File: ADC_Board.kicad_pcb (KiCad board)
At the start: 4 copper layers, 100 x 100 mm, 226 parts, among them J10 Wire_Solder_2Pin, J11 Wire_Solder_2Pin, J12 Wire_Solder_2Pin, J3 Conn_01x04_Pin, J4 Conn_01x04_Pin, J5 Conn_01x04_Pin, J6 Conn_01x04_Pin, J7 Wire_Solder_2Pin, J8 Wire_Solder_2Pin, J9 Conn_01x07_Socket, Q10 NVMFS5C468NL-HXY, Q11 NVMFS5C468NL-HXY, Q12 NVMFS5C468NL-HXY, Q4 DOD40P03, Q5 NVMFS5C468NL-HXY, Q6 NVMFS5C468NL-HXY, Q7 NVMFS5C468NL-HXY, Q8 NVMFS5C468NL-HXY, Q9 NVMFS5C468NL-HXY, SW1 SW_Push, U1 TPS70933DBVR, U10 INA281A3, U11 INA281A3, U12 INA281A3, U2 STM32G030K6Tx, U3 LM5109BMA, U4 LM5109BMA, U5 LM5109BMA, U6 LM5109BMA, U7 INA281A3, U8 SN74HCS08PWR, U9 SN74HCS02PWR, Y1 HSO321S 16MHZ 3.3V

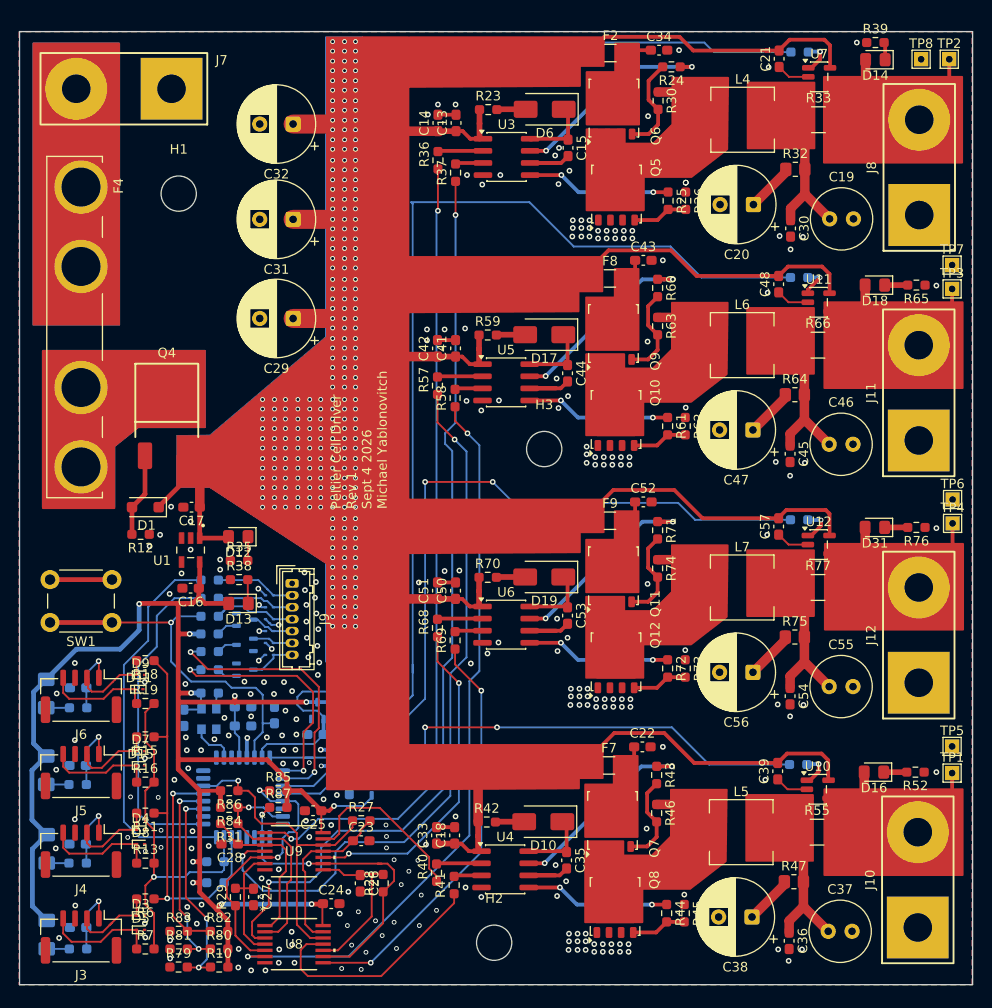
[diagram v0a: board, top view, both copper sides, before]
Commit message: changed I2C temp sensor to thermistor
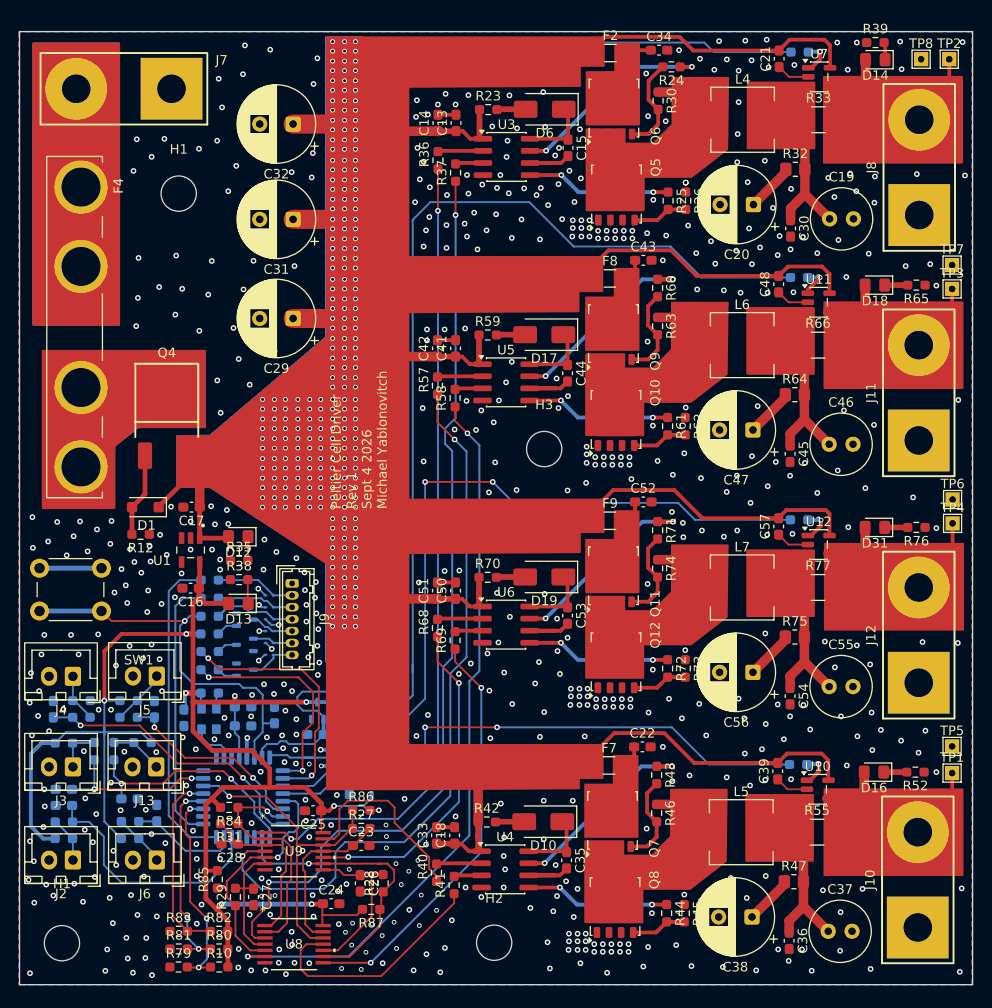
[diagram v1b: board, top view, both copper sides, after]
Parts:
- removed C11: 1u, Capacitor_SMD:C_0603_1608Metric_Pad1.08x0.95mm_HandSolder
- removed D11, D15, D3, D4, D5, D7, D8, D9: ESD9B3.3ST5G, Diode_SMD:D_SOD-923
- removed F1, F3, F5, F6: 25mA, Fuse:Fuse_1206_3216Metric_Pad1.42x1.75mm_HandSolder
- removed R16, R17, R18, R19, R20: 100r, Resistor_SMD:R_0603_1608Metric_Pad0.98x0.95mm_HandSolder
- removed R21, R22: 4.7k, Resistor_SMD:R_0603_1608Metric_Pad0.98x0.95mm_HandSolder
- added C1: 1u, Capacitor_SMD:C_0603_1608Metric_Pad1.08x0.95mm_HandSolder, B.Cu at (44.2, 152.7)
- added C2: 1u, Capacitor_SMD:C_0603_1608Metric_Pad1.08x0.95mm_HandSolder, B.Cu at (44.2, 151.0)
- added C3: 1u, Capacitor_SMD:C_0603_1608Metric_Pad1.08x0.95mm_HandSolder, B.Cu at (43.1, 142.6)
- added H1: MountingHole, MountingHole:MountingHole_3.7mm, F.Cu at (44.0, 167.2)
- added J13: Conn_01x02_Pin, Connector_JST:JST_XH_B2B-XH-A_1x02_P2.50mm_Vertical, F.Cu at (53.9, 148.7)
- added J2: Conn_01x02_Pin, Connector_JST:JST_XH_B2B-XH-A_1x02_P2.50mm_Vertical, F.Cu at (45.1, 158.4)
- added R1: 10k, Resistor_SMD:R_0603_1608Metric_Pad0.98x0.95mm_HandSolder, B.Cu at (44.2, 156.2)
- added R2: 1k, Resistor_SMD:R_0603_1608Metric_Pad0.98x0.95mm_HandSolder, B.Cu at (44.2, 154.4)
- added R3: 10k, Resistor_SMD:R_0603_1608Metric_Pad0.98x0.95mm_HandSolder, B.Cu at (44.2, 146.2)
- added R4: 1k, Resistor_SMD:R_0603_1608Metric_Pad0.98x0.95mm_HandSolder, B.Cu at (47.4, 147.0)
- added R5: 10k, Resistor_SMD:R_0603_1608Metric_Pad0.98x0.95mm_HandSolder, B.Cu at (46.0, 141.7)
- J3, J4, J5, J6: value Conn_01x04_Pin -> Conn_01x02_Pin; footprint Connector_JST:JST_GH_BM04B-GHS-TBT_1x04-1MP_P1.25mm_Vertical -> Connector_JST:JST_XH_B2B-XH-A_1x02_P2.50mm_Vertical
- R11, R7: value 100r -> 10k; moved to B.Cu
- R13, R15, R6: value 100r -> 1k; moved to B.Cu
- R14: value 100r -> 10k
- R8: value 100r -> 1k
- moved R7 26.1 mm to (51.0, 141.7), turned to 180 degrees
- moved R8 24.9 mm to (51.0, 143.4), turned to 0 degrees
- moved C5 24.3 mm to (53.7, 142.6), turned to 90 degrees
- moved R6 20.2 mm to (46.0, 143.4)
- moved J6 18.9 mm to (54.0, 158.4)
- moved J4 18.4 mm to (45.1, 139.2)
- moved J3 17.9 mm to (45.1, 148.7)
- moved R87 14.5 mm to (76.5, 163.6), turned to 180 degrees
- moved R14 14.4 mm to (52.5, 146.1), turned to 0 degrees
- moved R86 14.0 mm to (75.4, 153.2), turned to 0 degrees
- moved J5 12.9 mm to (54.0, 139.1)
- moved R85 11.3 mm to (60.3, 160.4), turned to 90 degrees
- moved C7 8.91 mm to (54.0, 153.5), turned to 90 degrees
- moved C10 6.48 mm to (51.1, 152.0), turned to 0 degrees
- moved R13 4.66 mm to (51.1, 154.4)
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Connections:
- net ADC_1 renamed ADC_MOTOR_CURRENT_1
- net ADC_2 renamed ADC_MOTOR_CURRENT_2
- net ADC_3 renamed ADC_MOTOR_CURRENT_3
- net ADC_4 renamed ADC_MOTOR_CURRENT_4
- C10 pad 1: Net-(J5-Pin_1) -> ADC_THERMISTOR_3
- C5 pad 1: Net-(J3-Pin_1) -> ADC_THERMISTOR_1
- C7 pad 1: Net-(J4-Pin_1) -> ADC_THERMISTOR_6
- J3 pad 2: Net-(D3-A1) -> GND
- J4 pad 2: Net-(D4-A1) -> GND
- J5 pad 2: Net-(D7-A1) -> GND
- J6 pad 2: Net-(D9-A1) -> GND
- R11 pad 1: I2C_SCL -> Net-(J6-Pin_1)
- R11 pad 2: Net-(D4-A1) -> +3.3V
- R13 pad 1: Net-(D8-A1) -> Net-(J6-Pin_1)
- R13 pad 2: I2C_SDA -> ADC_THERMISTOR_6
- R14 pad 1: Net-(J4-Pin_1) -> Net-(J13-Pin_1)
- R14 pad 2: Net-(F3-Pad1) -> +3.3V
- R15 pad 1: I2C_SCL -> Net-(J13-Pin_1)
- R15 pad 2: Net-(D7-A1) -> ADC_THERMISTOR_3
- R6 pad 1: I2C_SCL -> Net-(J4-Pin_1)
- R6 pad 2: Net-(D3-A1) -> ADC_THERMISTOR_2
- R7 pad 1: Net-(D5-A1) -> Net-(J5-Pin_1)
- R7 pad 2: I2C_SDA -> +3.3V
- R8 pad 1: Net-(J3-Pin_1) -> Net-(J5-Pin_1)
- R8 pad 2: Net-(F1-Pad1) -> ADC_THERMISTOR_1
- U2 pad 14: unconnected-(U2-PA7-Pad14) -> ADC_THERMISTOR_1
- U2 pad 16: unconnected-(U2-PB1-Pad16) -> ADC_THERMISTOR_2
- U2 pad 17: unconnected-(U2-PB2-Pad17) -> ADC_THERMISTOR_3
- U2 pad 22: I2C_SCL -> ADC_THERMISTOR_5
- U2 pad 23: I2C_SDA -> ADC_THERMISTOR_6
- U2 pad 31: unconnected-(U2-PB7-Pad31) -> ADC_THERMISTOR_4
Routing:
- net I2C_SCL: track 41.5 -> 0.00 mm, vias 1 -> 0
- net I2C_SDA: track 40.2 -> 0.00 mm, vias 1 -> 0
- net ADC_THERMISTOR_2: track 0.00 -> 29.8 mm, vias 0 -> 2
- net ADC_THERMISTOR_5: track 0.00 -> 26.1 mm
- net ADC_THERMISTOR_3: track 0.00 -> 24.7 mm, vias 0 -> 2
- net ADC_THERMISTOR_1: track 0.00 -> 20.5 mm, vias 0 -> 2
- net ADC_THERMISTOR_4: track 0.00 -> 17.3 mm, vias 0 -> 2
- net Net-(D5-A1): track 12.2 -> 0.00 mm
- net Net-(D8-A1): track 12.0 -> 0.00 mm
- net Net-(D15-A1): track 11.6 -> 0.00 mm
- net ADC_THERMISTOR_6: track 0.00 -> 11.4 mm
- net Net-(D11-A1): track 11.3 -> 0.00 mm
- net Net-(D3-A1): track 9.27 -> 0.00 mm
- net Net-(D4-A1): track 8.91 -> 0.00 mm
- net Net-(D9-A1): track 8.64 -> 0.00 mm
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
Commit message: Placed designators
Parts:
- renumbered C34 to C1, C30 to C10, C43 to C11, C48 to C12, C29 to C13, C42 to C14, C41 to C15, C44 to C16, C47 to C17, C46 to C18, C45 to C19, C21 to C2, C52 to C20, C17 to C21, C57 to C22, C16 to C23, C51 to C24, C50 to C25, C53 to C26, C56 to C27, C55 to C28, C54 to C29, C14 to C3, C22 to C30, C39 to C31, C25 to C32, C18 to C34, C28 to C35, C23 to C36, C35 to C37, C26 to C38, C27 to C39, C13 to C4, C24 to C40, C38 to C41, C37 to C42, C36 to C43, C6 to C44, C5 to C45, C3 to C46, C8 to C47, C9 to C48, C4 to C49, C32 to C5, C58 to C50, C59 to C51, C40 to C52, C49 to C53, C2 to C54, C10 to C55, C1 to C56, C7 to C57, C15 to C6, C20 to C7, C19 to C8, C31 to C9, D14 to D1, D16 to D10, D10 to D11, D23 to D12, D22 to D13, D21 to D14, D27 to D15, D20 to D16, D25 to D17, D2 to D18, D24 to D19, D6 to D2, D26 to D20, D35 to D21, D29 to D22, D34 to D23, D32 to D24, D18 to D3, D17 to D4, D1 to D5, D31 to D6, D12 to D7, D19 to D8, D13 to D9, F2 to F1, F8 to F2, F4 to F3, F9 to F4, F7 to F5, H3 to H2, H2 to H3, H1 to H4, J7 to J1, J2 to J10, J6 to J11, J10 to J12, J8 to J2, J11 to J3, J9 to J4, J4 to J6, J12 to J7, J3 to J8, J13 to J9, L4 to L1, L6 to L2, L7 to L3, L5 to L4, Q6 to Q1, Q5 to Q2, Q9 to Q3, Q10 to Q5, Q11 to Q6, Q12 to Q7, Q7 to Q8, Q8 to Q9, R39 to R1, R26 to R10, R65 to R11, R60 to R12, R63 to R13, R59 to R14, R66 to R15, R57 to R16, R64 to R17, R58 to R18, R61 to R19, R24 to R2, R62 to R20, R76 to R21, R71 to R22, R12 to R23, R35 to R24, R74 to R25, R70 to R26, R38 to R27, R77 to R28, R68 to R29, R30 to R3, R75 to R30, R69 to R31, R72 to R32, R73 to R33, R52 to R34, R43 to R35, R84 to R36, R86 to R37, R46 to R38, R42 to R39, R23 to R4, R31 to R40, R27 to R41, R55 to R42, R40 to R43, R85 to R44, R47 to R45, R28 to R46, R41 to R47, R29 to R48, R87 to R49, R33 to R5, R44 to R50, R45 to R51, R83 to R52, R82 to R53, R81 to R54, R80 to R55, R79 to R56, R10 to R57, R34 to R58, R67 to R59, R36 to R6, R78 to R60, R50 to R61, R49 to R62, R48 to R63, R54 to R64, R51 to R65, R53 to R66, R9 to R67, R7 to R68, R5 to R69, R32 to R7, R8 to R70, R6 to R71, R14 to R72, R3 to R73, R15 to R74, R4 to R75, R56 to R76, R13 to R77, R2 to R78, R11 to R79, R37 to R8, R1 to R80, R25 to R9, TP8 to TP1, TP7 to TP3, TP3 to TP4, TP6 to TP5, TP4 to TP6, TP5 to TP7, TP1 to TP8, U7 to U1, U4 to U10, U8 to U11, U2 to U12, U3 to U2, U11 to U3, U5 to U4, U12 to U5, U1 to U6, U6 to U7, U10 to U8
